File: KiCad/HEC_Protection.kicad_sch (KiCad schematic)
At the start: 11 parts, among them U11 74LS00, U11 74LS32, U12 74LS04, U17 74LS74, U18 74LS74, U19 74LS30, U23 74LS30, U25 74LS541, U26 74LS541, U28 74LS20

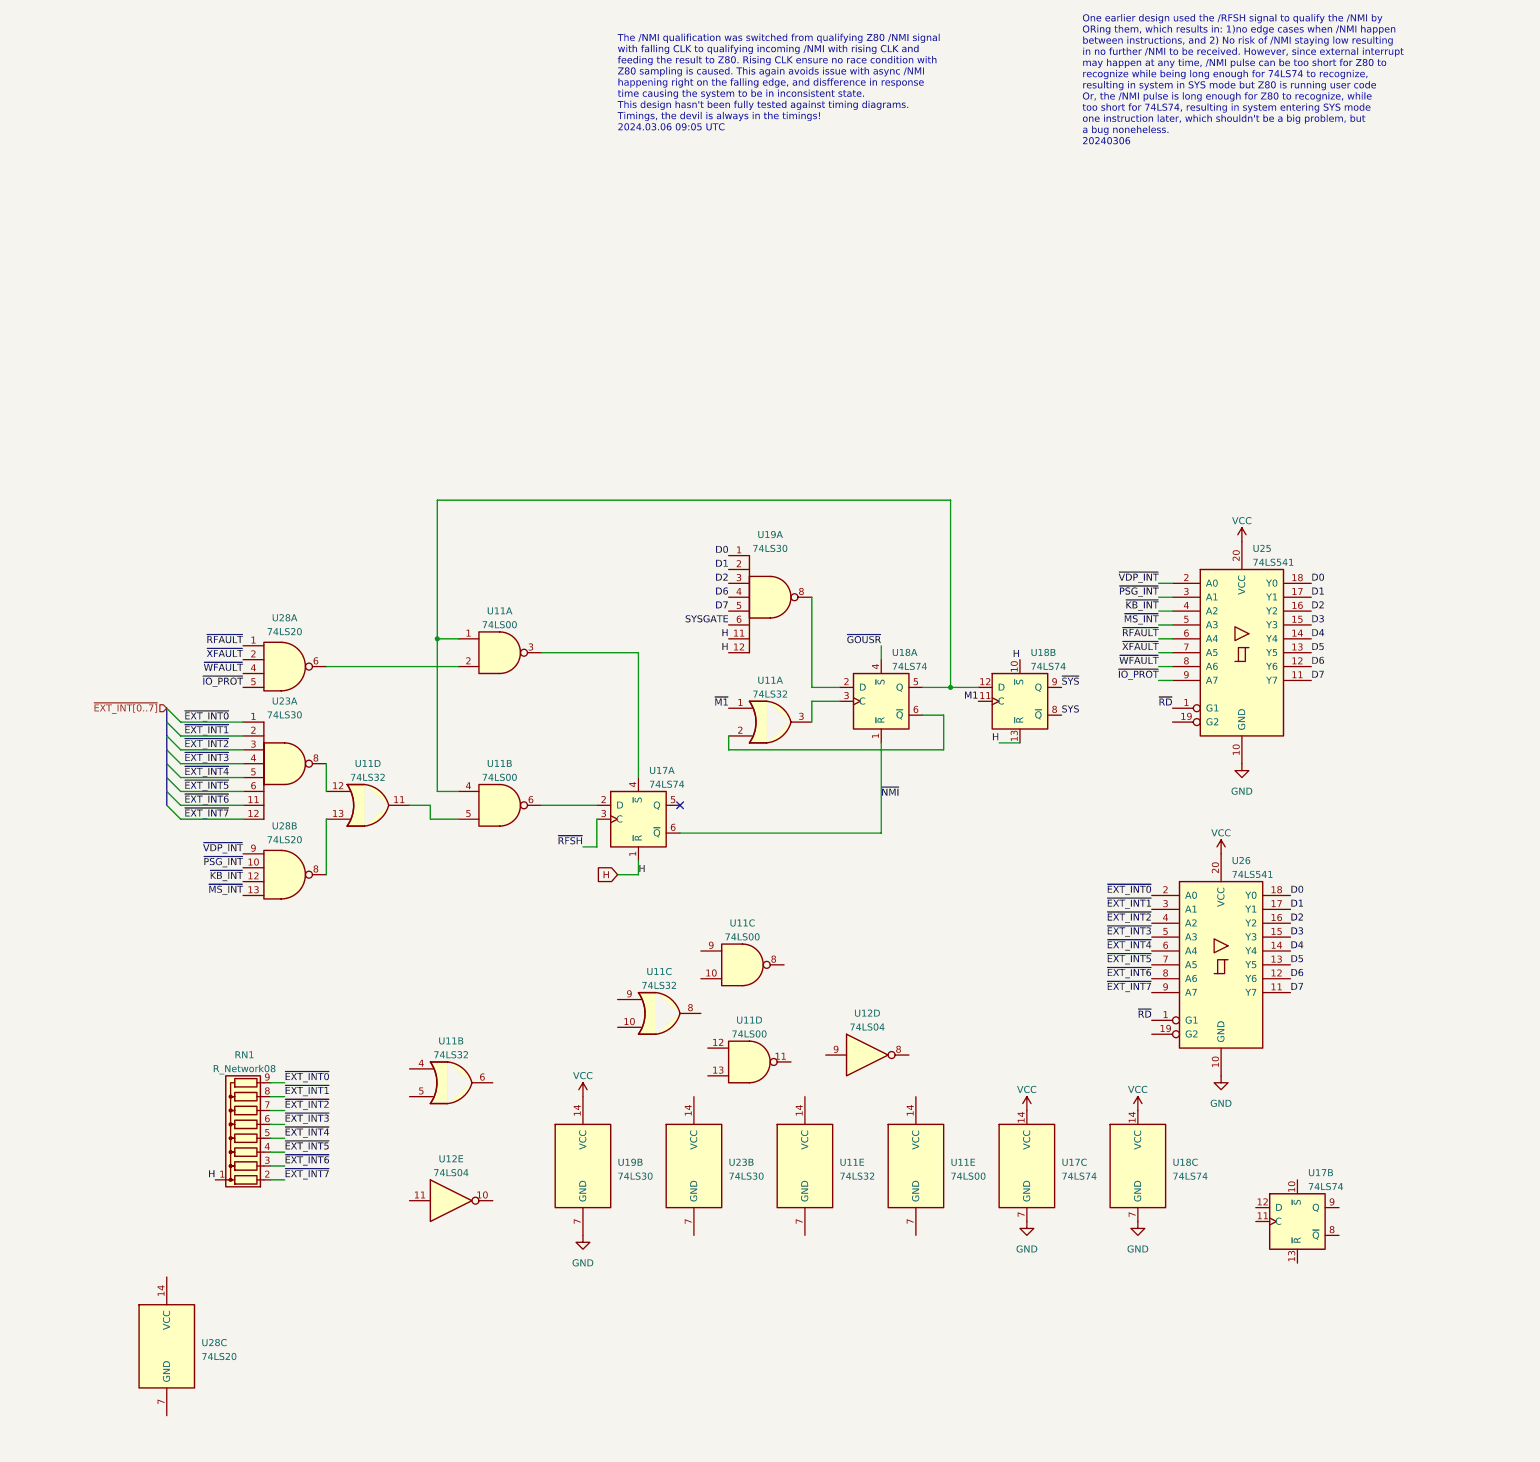
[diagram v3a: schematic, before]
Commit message: Add fault generation circuit
Add circuit to generate fault on illegal read, write and M1 cycle
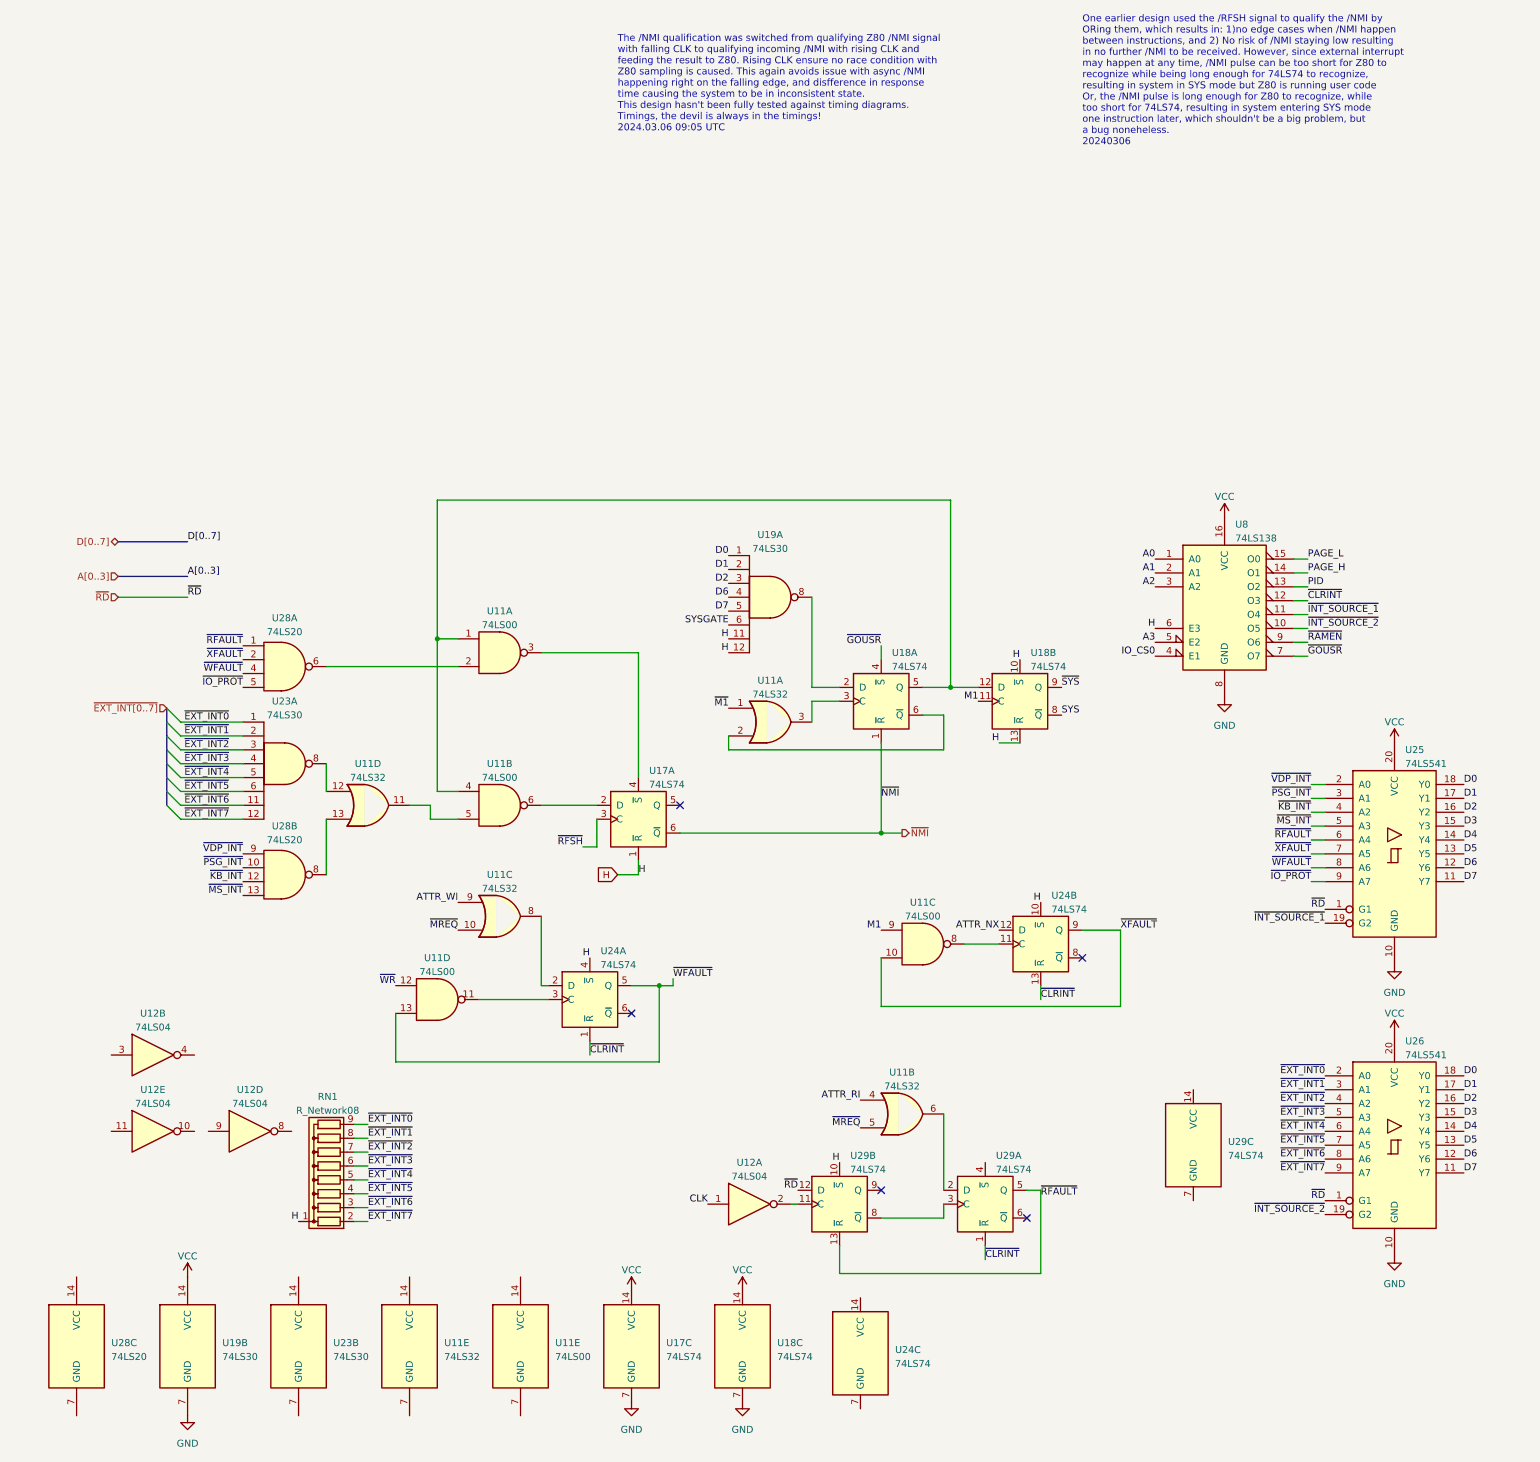
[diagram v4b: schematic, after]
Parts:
- removed unit 2 of U17
- added unit 1 of U12
- added unit 2 of U12
- added U24, U29: 74LS74, symbol 74xx:74LS74
- added U8: 74LS138, Package_DIP:DIP-16_W7.62mm_Socket, symbol 74xx:74LS138
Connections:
- net GND: now also U8.8 (GND)
- net H: now also U24.10 (~{S}), U24.4 (~{S}), U29.10 (~{S}), U8.6 (E3)
- net M1: now also U11.9
- net VCC: now also U8.16 (VCC)
- net ~{GOUSR}: now also U8.7 (O7)
- net ~{RD}: now also U29.12 (D)
- net ~{RFAULT}: now also U29.13 (~{R}), U29.5 (Q)
- net ~{WFAULT}: now also U11.13, U24.5 (Q)
- net ~{XFAULT}: now also U11.10, U24.9 (Q)
- net ATTR_RI: now reaches U11.4
- net ~{MREQ}: now reaches U11.5
- net ~{MREQ}: now also U11.10
- net at U11.6: now also U29.2 (D)
- net at U11.8: now also U24.11 (C)
- net at U11.8: now also U24.2 (D)
- net ATTR_WI: now reaches U11.9
- net ~{INT_SOURCE_1}: now reaches U25.19 (G2)
- net ~{INT_SOURCE_1}: now also U8.11 (O4)
- net at U11.11: now also U24.3 (C)
- net ~{WR}: now reaches U11.12
- net ~{INT_SOURCE_2}: now reaches U26.19 (G2)
- net ~{INT_SOURCE_2}: now also U8.10 (O5)
- new net: U12.2, U29.11 (C)
- new net: U29.3 (C), U29.8 (~{Q})
- new net A0: U8.1 (A0)
- new net A1: U8.2 (A1)
- new net A2: U8.3 (A2)
- new net A3: U8.5 (E2)
- new net ATTR_NX: U24.12 (D)
- new net CLK: U12.1
- new net IO_CS0: U8.4 (E1)
- new net PAGE_H: U8.14 (O1)
- new net PAGE_L: U8.15 (O0)
- new net PID: U8.13 (O2)
- new net ~{CLRINT}: U24.1 (~{R}), U24.13 (~{R}), U29.1 (~{R}), U8.12 (O3)
- new net ~{RAMEN}: U8.9 (O6)
- no-connect marks 1 -> 5
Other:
- moved on the sheet: RN1, U11B, U11C, U11D, U11E, U12D, U12E, U17C, U18C, U19B, U23B, U25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

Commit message: Complete fault generation circuit
Add circuit to generate fault on illegal IO access. The protection circuit design is not considered complete.
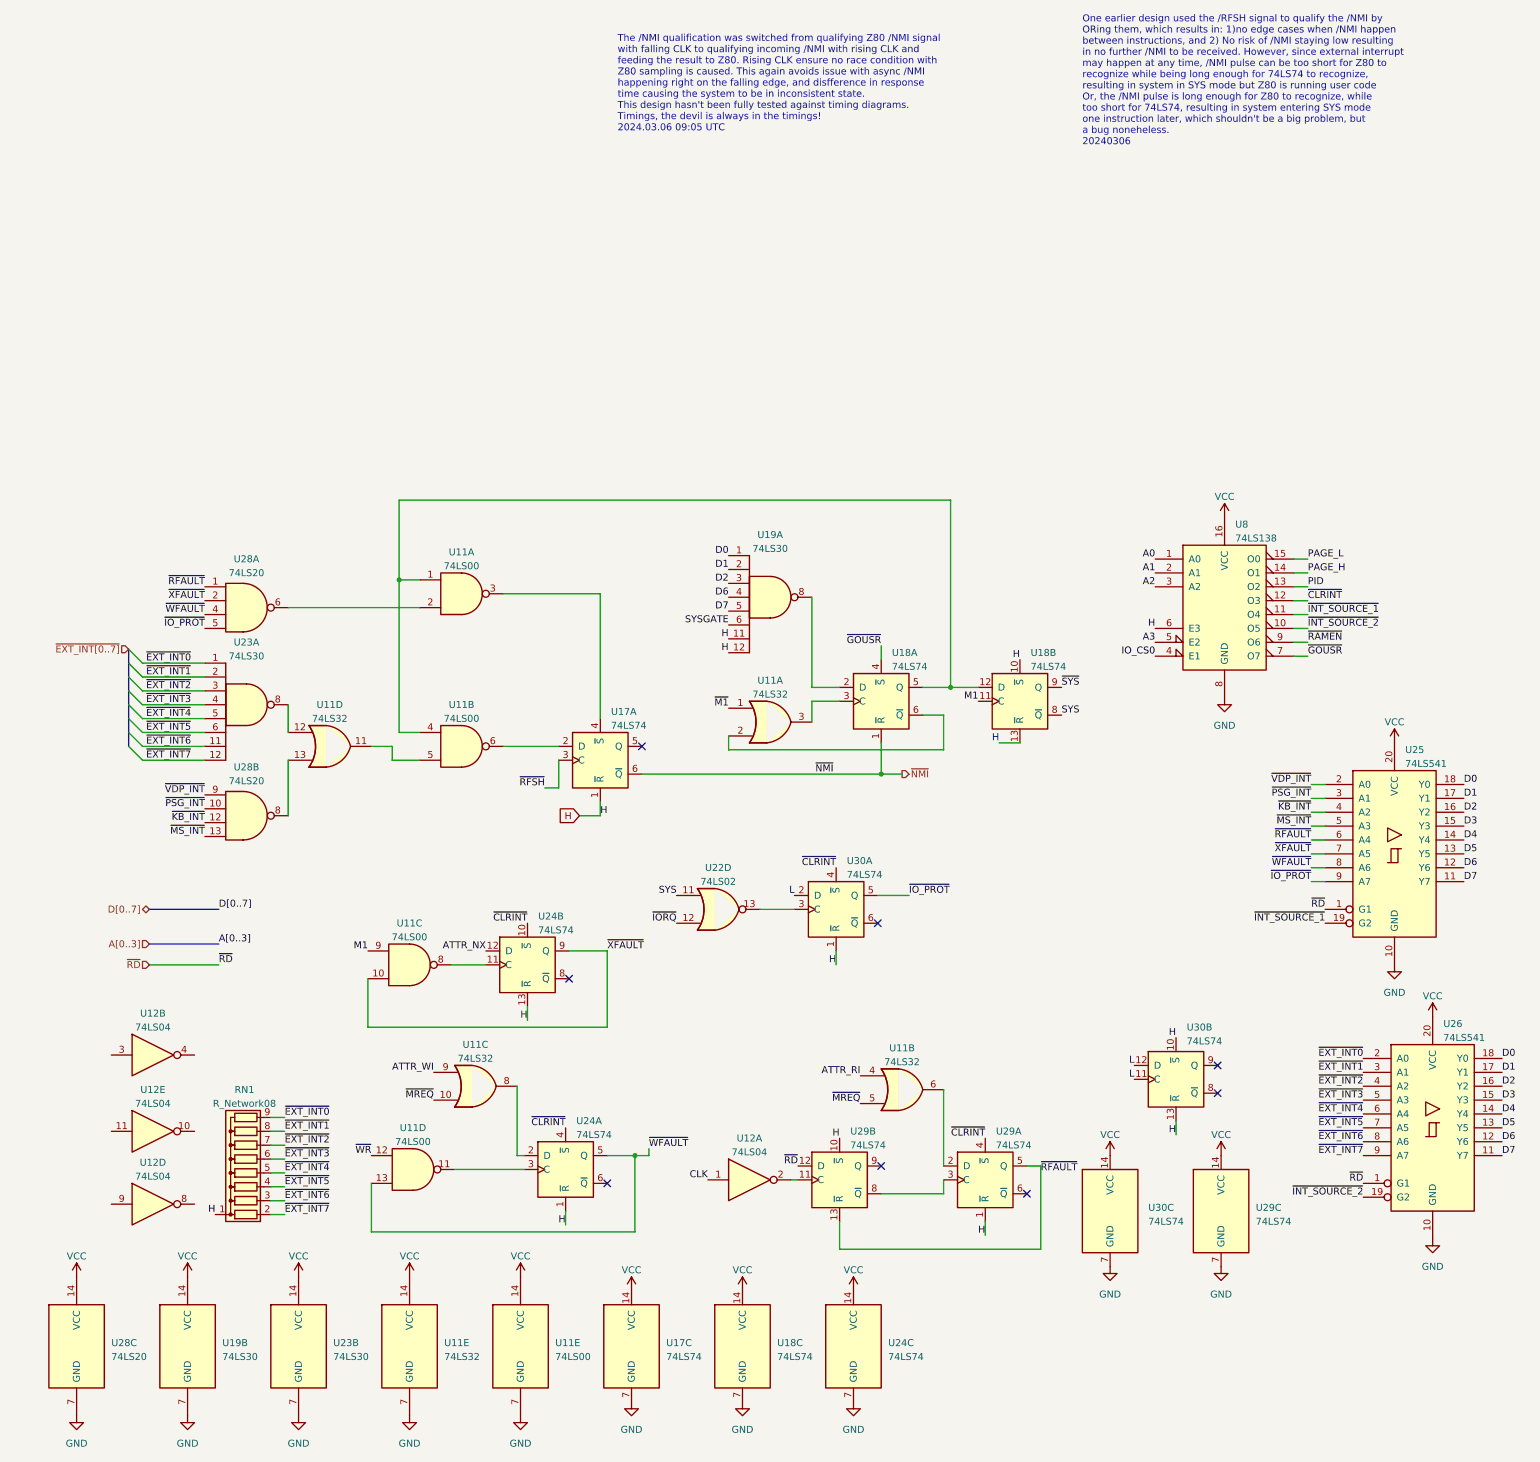
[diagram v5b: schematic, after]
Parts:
- added U22: 74LS02, Package_DIP:DIP-14_W7.62mm_Socket, symbol 74xx:74LS02
- added U30: 74LS74, symbol 74xx:74LS74
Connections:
- net GND: now also U11.7 (GND), U11.7 (GND), U23.7 (GND), U24.7 (GND), U28.7 (GND), U29.7 (GND), U30.7 (GND)
- net H: now also U24.1 (~{R}), U24.13 (~{R}), U29.1 (~{R}), U30.1 (~{R}), U30.10 (~{S}), U30.13 (~{R}); no longer U24.10 (~{S}), U24.4 (~{S})
- net SYS: now also U22.11
- net VCC: now also U11.14 (VCC), U11.14 (VCC), U23.14 (VCC), U24.14 (VCC), U28.14 (VCC), U29.14 (VCC), U30.14 (VCC)
- net ~{CLRINT}: now also U24.10 (~{S}), U24.4 (~{S}), U29.4 (~{S}), U30.4 (~{S}); no longer U24.1 (~{R}), U24.13 (~{R}), U29.1 (~{R})
- net ~{IO_PROT}: now also U30.5 (Q)
- new net: U22.13, U30.3 (C)
- new net L: U30.11 (C), U30.12 (D), U30.2 (D)
- new net ~{IORQ}: U22.12
- no-connect marks 5 -> 8
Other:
- moved on the sheet: RN1, U11A, U11B, U11C, U11D, U12A, U12D, U17A, U23A, U24A, U24B, U24C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

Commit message: Created footprint for HEC bus
Created footprints for HEC bus and some other updates.
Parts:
- U11, U24, U28, U29, U30: footprint (none) -> Package_DIP:DIP-14_W7.62mm_Socket
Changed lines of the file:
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@@
       (effects (font (size 1.27 1.27)) (justify left))
     )
-    (property "Footprint" "" (at 158.75 143.51 0)
+    (property "Footprint" "Package_DIP:DIP-14_W7.62mm_Socket" (at 158.75 143.51 0)
       (effects (font (size 1.27 1.27)) hide)
     )
@@
       (effects (font (size 1.27 1.27)) (justify left))
     )
-    (property "Footprint" "" (at 208.28 149.225 0)
+    (property "Footprint" "Package_DIP:DIP-14_W7.62mm_Socket" (at 208.28 149.225 0)
       (effects (font (size 1.27 1.27)) hide)
     )
@@
       (effects (font (size 1.27 1.27)))
     )
-    (property "Footprint" "" (at 80.01 104.14 0)
+    (property "Footprint" "Package_DIP:DIP-14_W7.62mm_Socket" (at 80.01 104.14 0)
       (effects (font (size 1.27 1.27)) hide)
     )
@@
       (effects (font (size 1.27 1.27)) (justify left))
     )
-    (property "Footprint" "" (at 19.05 173.99 0)
+    (property "Footprint" "Package_DIP:DIP-14_W7.62mm_Socket" (at 19.05 173.99 0)
       (effects (font (size 1.27 1.27)) hide)
     )
@@
       (effects (font (size 1.27 1.27)))
     )
-    (property "Footprint" "" (at 89.535 36.195 0)
+    (property "Footprint" "Package_DIP:DIP-14_W7.62mm_Socket" (at 89.535 36.195 0)
       (effects (font (size 1.27 1.27)) hide)
     )
@@
       (effects (font (size 1.27 1.27)) (justify left))
     )
-    (property "Footprint" "" (at 228.6 149.225 0)
+    (property "Footprint" "Package_DIP:DIP-14_W7.62mm_Socket" (at 228.6 149.225 0)
       (effects (font (size 1.27 1.27)) hide)
     )
@@
       (effects (font (size 1.27 1.27)))
     )
-    (property "Footprint" "" (at 50.165 76.835 0)
+    (property "Footprint" "Package_DIP:DIP-14_W7.62mm_Socket" (at 50.165 76.835 0)
       (effects (font (size 1.27 1.27)) hide)
     )
@@
       (effects (font (size 1.27 1.27)) (justify left))
     )
-    (property "Footprint" "" (at 101.6 104.14 0)
+    (property "Footprint" "Package_DIP:DIP-14_W7.62mm_Socket" (at 101.6 104.14 0)
       (effects (font (size 1.27 1.27)) hide)
     )
@@
       (effects (font (size 1.27 1.27)))
     )
-    (property "Footprint" "" (at 80.645 141.605 0)
+    (property "Footprint" "Package_DIP:DIP-14_W7.62mm_Socket" (at 80.645 141.605 0)
       (effects (font (size 1.27 1.27)) hide)
     )
@@
       (effects (font (size 1.27 1.27)) (justify left))
     )
-    (property "Footprint" "" (at 185.42 143.51 0)
+    (property "Footprint" "Package_DIP:DIP-14_W7.62mm_Socket" (at 185.42 143.51 0)
       (effects (font (size 1.27 1.27)) hide)
     )
@@
       (effects (font (size 1.27 1.27)) (justify left))
     )
-    (property "Footprint" "" (at 161.29 173.99 0)
+    (property "Footprint" "Package_DIP:DIP-14_W7.62mm_Socket" (at 161.29 173.99 0)
       (effects (font (size 1.27 1.27)) hide)
     )
@@
       (effects (font (size 1.27 1.27)))
     )
-    (property "Footprint" "" (at 50.165 38.735 0)
+    (property "Footprint" "Package_DIP:DIP-14_W7.62mm_Socket" (at 50.165 38.735 0)
       (effects (font (size 1.27 1.27)) hide)
     )
@@
       (effects (font (size 1.27 1.27)) (justify left))
     )
-    (property "Footprint" "" (at 100.33 173.99 0)
+    (property "Footprint" "Package_DIP:DIP-14_W7.62mm_Socket" (at 100.33 173.99 0)
       (effects (font (size 1.27 1.27)) hide)
     )
@@
       (effects (font (size 1.27 1.27)) (justify left))
     )
-    (property "Footprint" "" (at 220.345 125.095 0)
+    (property "Footprint" "Package_DIP:DIP-14_W7.62mm_Socket" (at 220.345 125.095 0)
       (effects (font (size 1.27 1.27)) hide)
     )
@@
       (effects (font (size 1.27 1.27)))
     )
-    (property "Footprint" "" (at 89.535 64.135 0)
+    (property "Footprint" "Package_DIP:DIP-14_W7.62mm_Socket" (at 89.535 64.135 0)
       (effects (font (size 1.27 1.27)) hide)
     )
@@
       (effects (font (size 1.27 1.27)) (justify left))
     )
-    (property "Footprint" "" (at 108.585 141.605 0)
+    (property "Footprint" "Package_DIP:DIP-14_W7.62mm_Socket" (at 108.585 141.605 0)
       (effects (font (size 1.27 1.27)) hide)
     )
@@
       (effects (font (size 1.27 1.27)) (justify left))
     )
-    (property "Footprint" "" (at 158.115 93.98 0)
-      (effects (font (size 1.27 1.27)) hide)
-    )
+    (property "Footprint" "Package_DIP:DIP-14_W7.62mm_Socket" (at 158.115 93.98 0)
+      (effects (font (size 1.27 1.27)) hide)
+    )
